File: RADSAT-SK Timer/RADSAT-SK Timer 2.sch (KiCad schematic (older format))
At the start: 50 parts, among them J201 Conn_01x07, J202 Conn_01x05, J203 Conn_01x03, J204 Conn_01x02, J205 Conn_01x02, J206 Conn_01x02, J210 ZX62WRD-B-5PC, Q201 IRLML2060, Q202 IRLML2060, Q203 IRLML2060, Q204 IRLML2060, Q205 IRLML2060, Q206 IRLML2060, SW201 SW_Push, SW202 SW_Push, SW203 SW_Push, SW204 SW_Push, SW205 SW_Push, SW206 SW_Push, U202 LTC3440EMSPBF, U230 CPC1117N, U240 CPC1117N, U250 CPC1117N, U260 CPC1117N

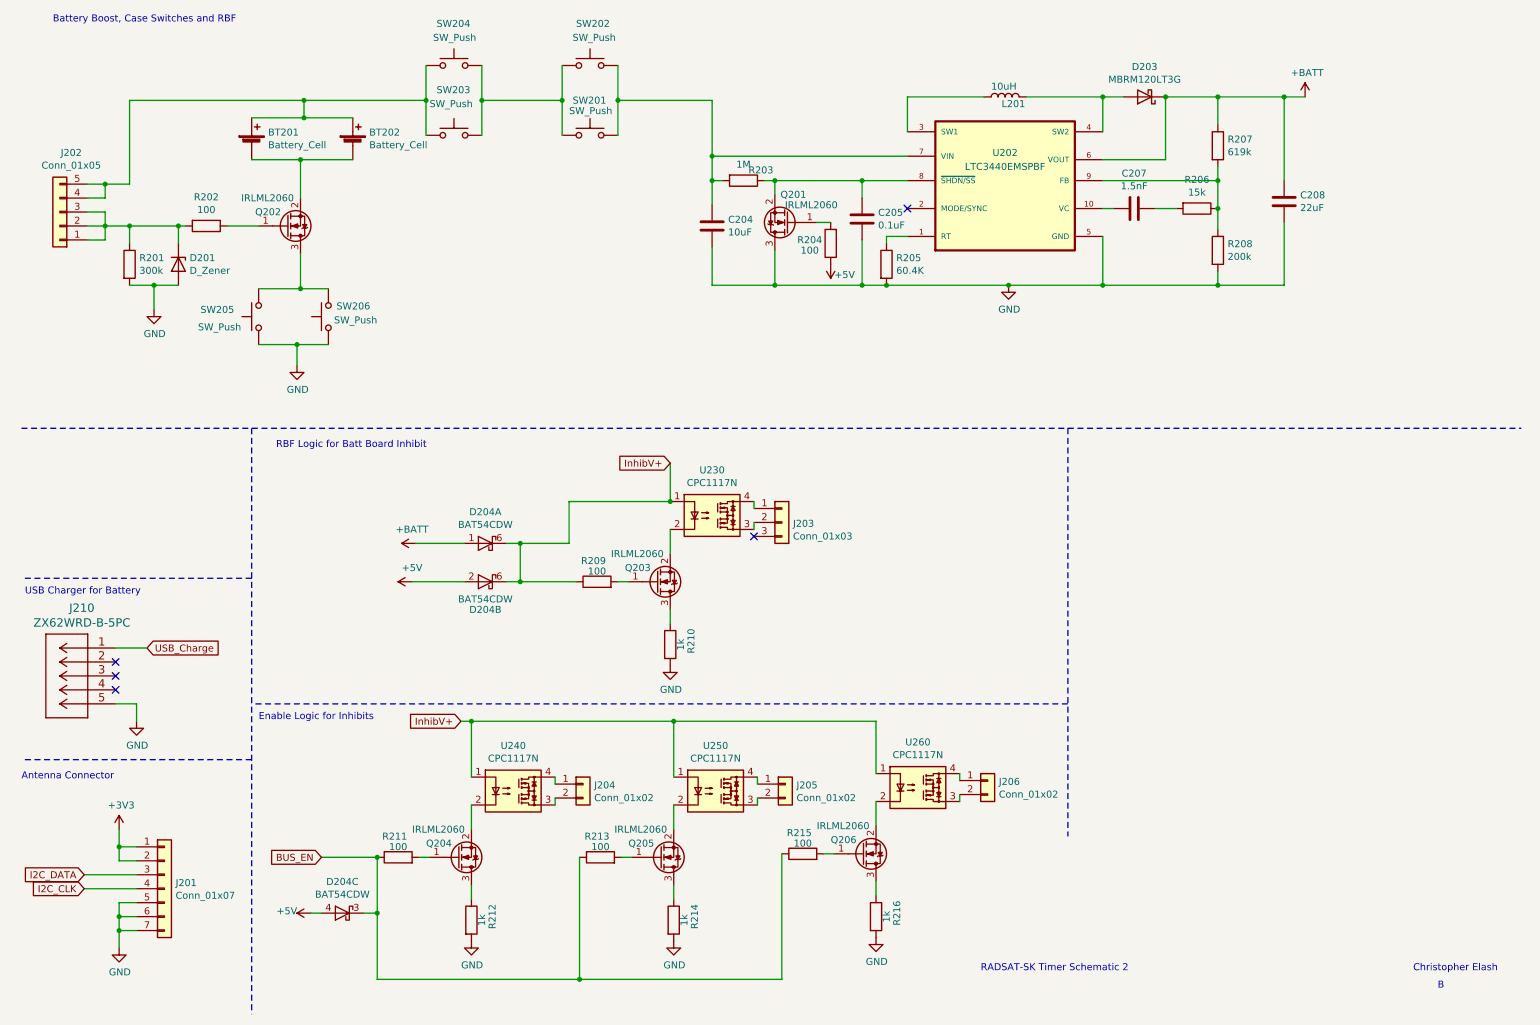
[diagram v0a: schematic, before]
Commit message: Noticed that the source on all of the schematic 2 transistors were wrong and needed to be flipped, except on the rbf where it is intentional q Q ~
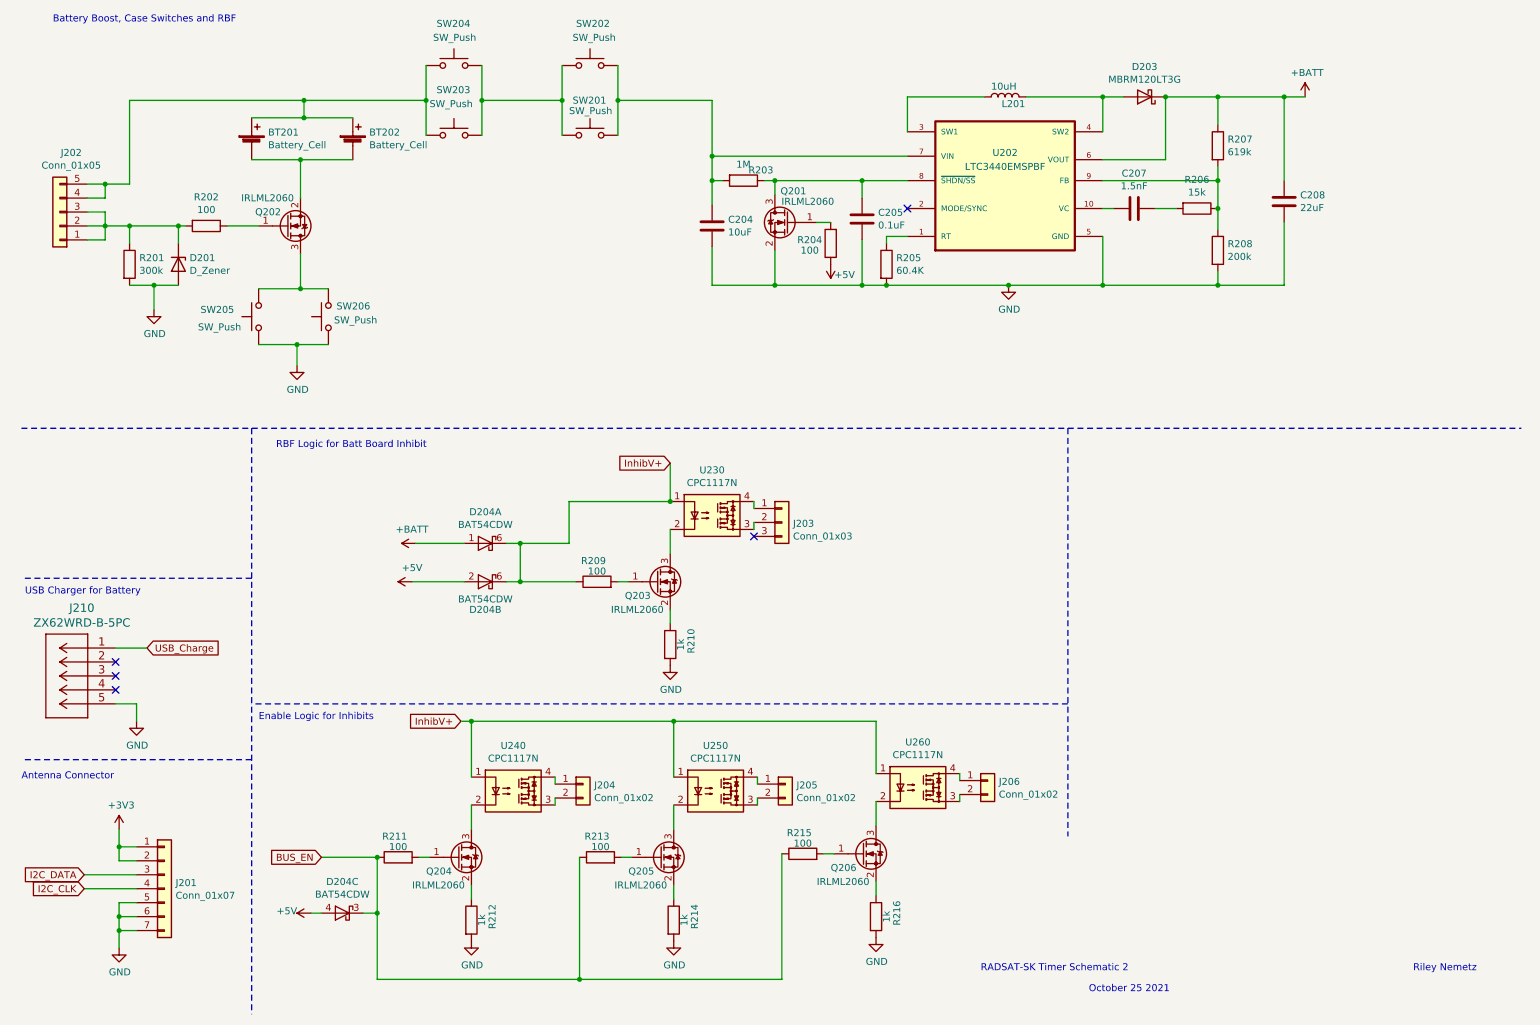
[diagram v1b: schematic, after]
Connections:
- net GND: now also Q201.2 (S); no longer Q201.3 (D)
- net at C205.1, R203.1, U202.8 (~SHDN/SS): now also Q201.3 (D); no longer Q201.2 (S)
- net at Q203.2 (S): now also R210.1; no longer U230.2
- net at Q203.3 (D): now also U230.2; no longer R210.1
- net at Q205.2 (S): now also R214.1; no longer U250.2
- net at Q205.3 (D): now also U250.2; no longer R214.1
- net at Q206.2 (S): now also R216.1; no longer U260.2
- net at Q206.3 (D): now also U260.2; no longer R216.1
- net at Q204.2 (S): now also R212.1; no longer U240.2
- net at Q204.3 (D): now also U240.2; no longer R212.1
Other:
- note added: "October 25 2021"
- note added: "Riley Nemetz"
- note removed: "B"
- note removed: "Christopher Elash"
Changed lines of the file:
@@
 AR Path="/600FFF1C" Ref="Q201"  Part="1"
 AR Path="/602E25D3/600FFF1C" Ref="Q201"  Part="1"
-F 0 "Q201" H 5850 1925 50  0000 L CNN
-F 1 "IRLML2060" H 5625 2000 50  0000 L CNN
+F 0 "Q201" H 5850 2350 50  0000 L CNN
+F 1 "IRLML2060" H 5650 2275 50  0000 L CNN
 F 2 "Package_TO_SOT_SMD:SOT-23_Handsoldering" H 6175 2050 50  0001 L CIN
 F 3 "https://www.infineon.com/dgdl/irlml2060pbf.pdf?fileId=5546d462533600a401535664b7fb25ee" H 5975 2125 50  0001 L CNN
 	1    5975 2125
-	-1   0    0    1
+	-1   0    0    -1
 $EndComp
 Connection ~ 6675 2575
@@
 	2500 1375 2850 1375
 Text Notes 10450 7500 0    50   ~ 0
-Christopher Elash
-Text Notes 10625 7625 0    50   ~ 0
-B
+Riley Nemetz
 Text Notes 700  700  0    50   ~ 0
 Battery Boost, Case Switches and RBF
@@
 F 3 "https://www.infineon.com/dgdl/irlml2060pbf.pdf?fileId=5546d462533600a401535664b7fb25ee" H 5025 4700 50  0001 L CNN
 	1    5025 4700
-	1    0    0    1
+	1    0    0    -1
 $EndComp
 $Comp
@@
 F 3 "https://www.infineon.com/dgdl/irlml2060pbf.pdf?fileId=5546d462533600a401535664b7fb25ee" H 6500 6650 50  0001 L CNN
 	1    6500 6650
-	1    0    0    1
+	1    0    0    -1
 $EndComp
 $Comp
@@
 F 3 "https://www.infineon.com/dgdl/irlml2060pbf.pdf?fileId=5546d462533600a401535664b7fb25ee" H 3600 6675 50  0001 L CNN
 	1    3600 6675
-	1    0    0    1
+	1    0    0    -1
 $EndComp
 Wire Wire Line
@@
 F 3 "https://www.infineon.com/dgdl/irlml2060pbf.pdf?fileId=5546d462533600a401535664b7fb25ee" H 5050 6675 50  0001 L CNN
 	1    5050 6675
-	1    0    0    1
+	1    0    0    -1
 $EndComp
 $Comp
@@
 	1    0    0    -1
 $EndComp
+Text Notes 8125 7650 0    50   ~ 0
+October 25 2021
 $EndSCHEMATC

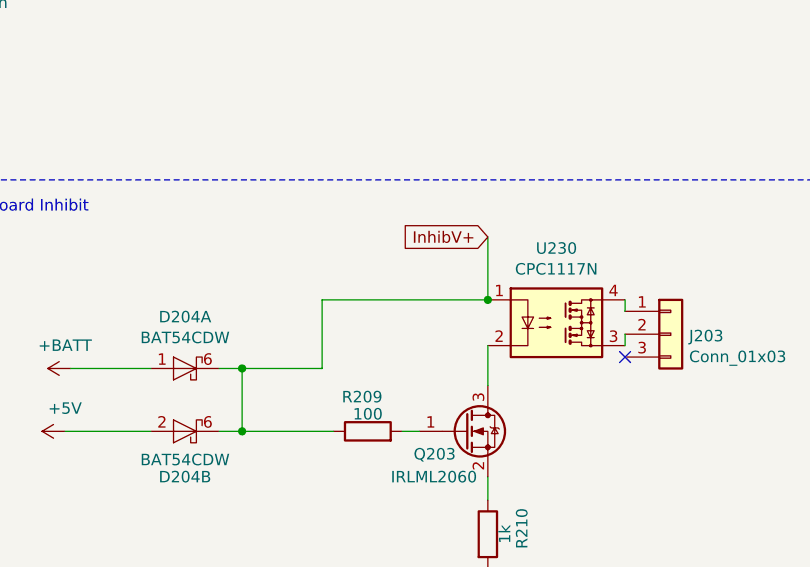
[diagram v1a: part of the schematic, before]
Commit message: Sourced coin cell battery and tantalum caps, still need to footprint coin cell holders
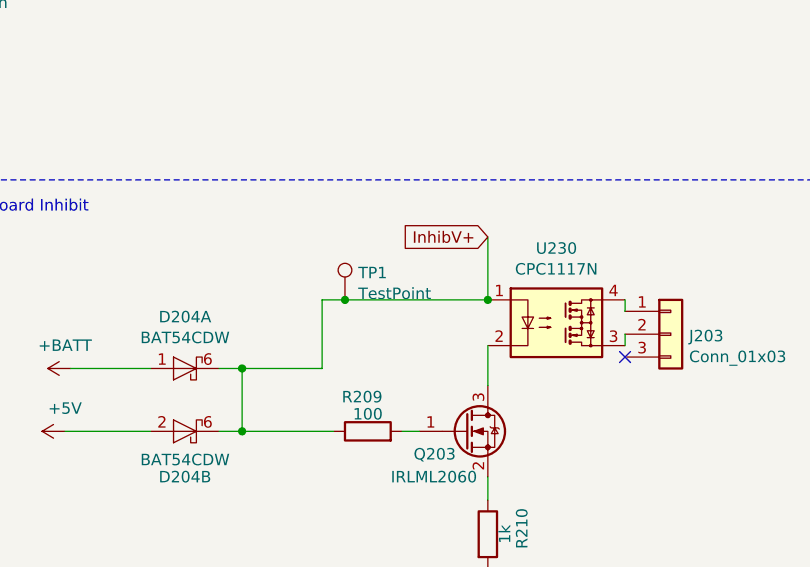
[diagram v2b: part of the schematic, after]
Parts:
- added TP1: TestPoint, TestPoint:TestPoint_Pad_D3.0mm, symbol Connector:TestPoint
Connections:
- net InhibV+: now also TP1.1
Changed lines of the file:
@@
 $EndComp
 $Comp
-L power:GND #PWR?
+L power:GND #PWR0119
 U 1 1 6182F8D4
 P 6600 7250
-F 0 "#PWR?" H 6600 7000 50  0001 C CNN
+F 0 "#PWR0119" H 6600 7000 50  0001 C CNN
 F 1 "GND" H 6605 7077 50  0000 C CNN
 F 2 "" H 6600 7250 50  0001 C CNN
@@
 $EndComp
 $Comp
-L power:GND #PWR?
+L power:GND #PWR0120
 U 1 1 6183DF37
 P 3700 7275
-F 0 "#PWR?" H 3700 7025 50  0001 C CNN
+F 0 "#PWR0120" H 3700 7025 50  0001 C CNN
 F 1 "GND" H 3705 7102 50  0000 C CNN
 F 2 "" H 3700 7275 50  0001 C CNN
@@
 	4775 6675 4850 6675
 $Comp
-L power:GND #PWR?
+L power:GND #PWR0121
 U 1 1 6181C5BF
 P 5150 7275
-F 0 "#PWR?" H 5150 7025 50  0001 C CNN
+F 0 "#PWR0121" H 5150 7025 50  0001 C CNN
 F 1 "GND" H 5155 7102 50  0000 C CNN
 F 2 "" H 5150 7275 50  0001 C CNN
@@
 	4400 4425 4400 4125
 Wire Wire Line
-	4400 4125 5125 4125
+	4400 4125 4500 4125
 Wire Wire Line
 	4050 4425 4400 4425
@@
 Text Notes 8125 7650 0    50   ~ 0
 October 25 2021
+$Comp
+L Connector:TestPoint TP1
+U 1 1 617A6F6B
+P 4500 4125
+F 0 "TP1" H 4558 4243 50  0000 L CNN
+F 1 "TestPoint" H 4558 4152 50  0000 L CNN
+F 2 "TestPoint:TestPoint_Pad_D3.0mm" H 4700 4125 50  0001 C CNN
+F 3 "~" H 4700 4125 50  0001 C CNN
+	1    4500 4125
+	1    0    0    -1
+$EndComp
+Connection ~ 4500 4125
+Wire Wire Line
+	4500 4125 5125 4125
 $EndSCHEMATC

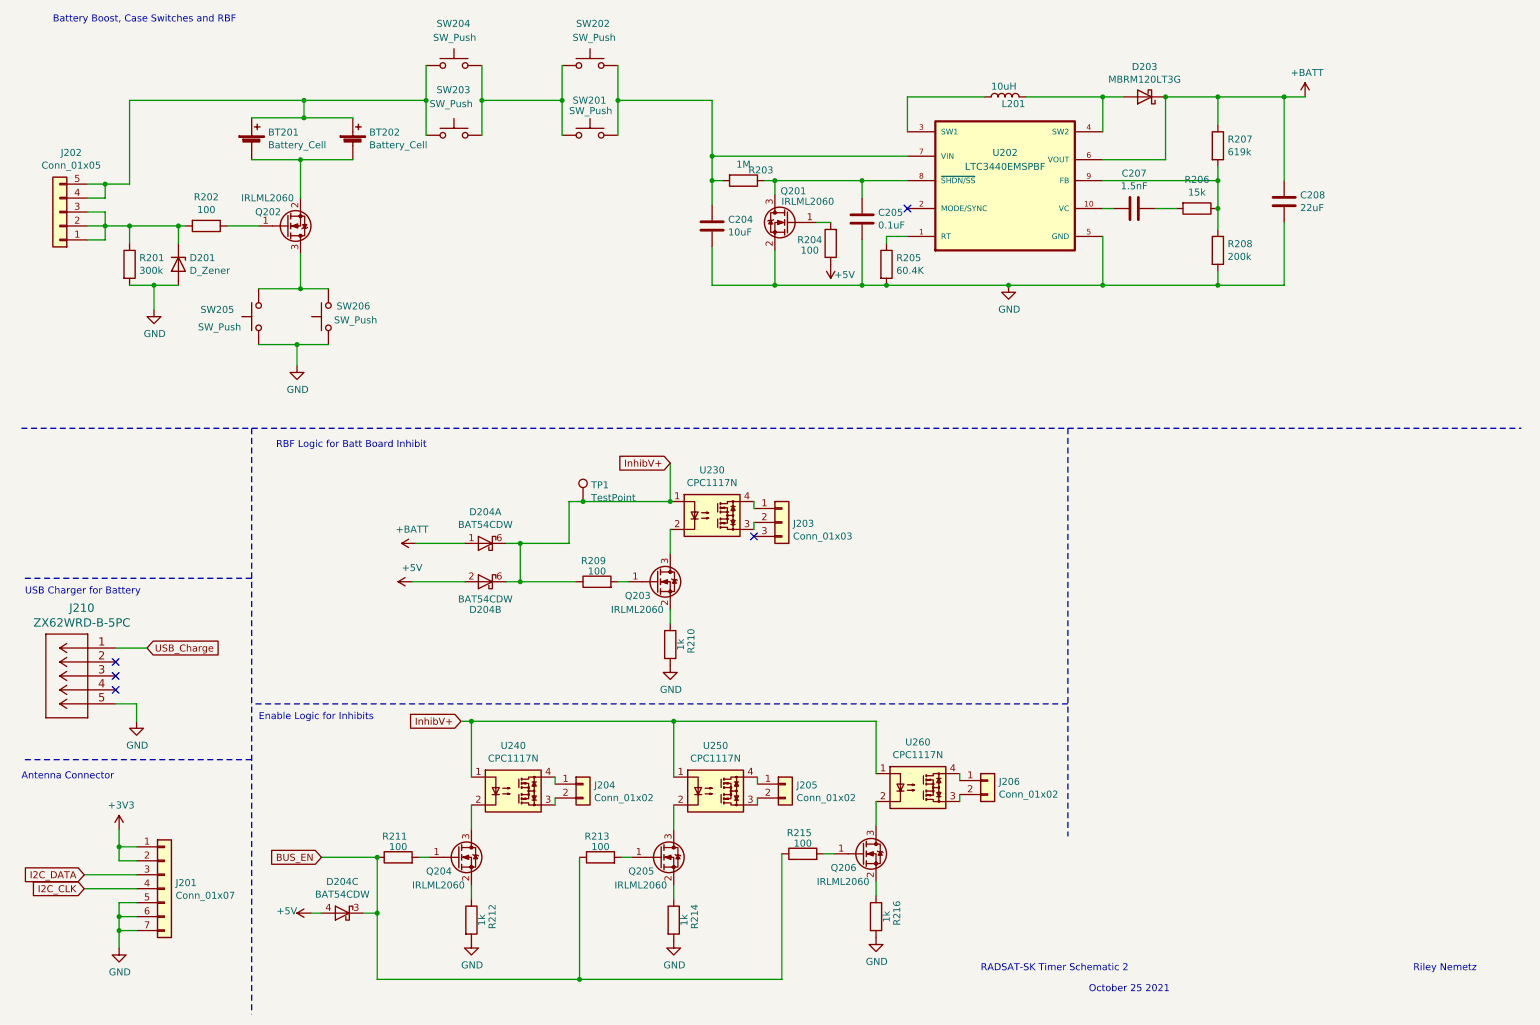
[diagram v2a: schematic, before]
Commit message: the RBF relay transistor was redundant, added in another LED and updated diode configuration, resistor sourcing TBD
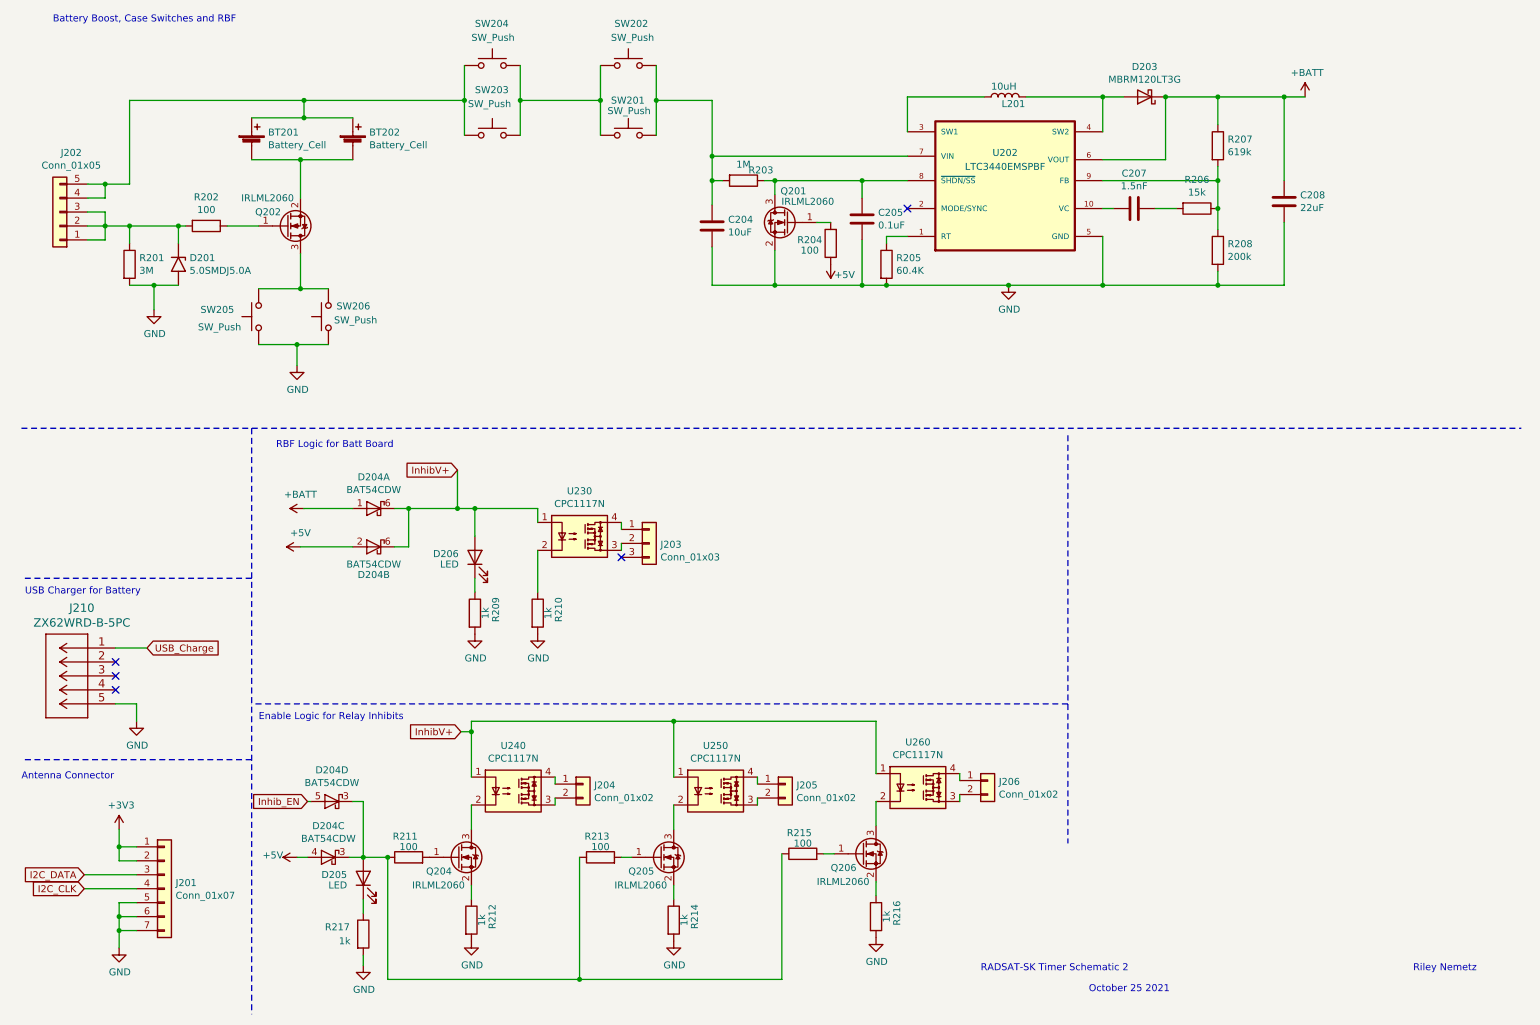
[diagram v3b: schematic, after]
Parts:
- removed D201: D_Zener, Diode_SMD:D_0805_2012Metric, symbol Device:D_Zener
- removed Q203: IRLML2060, Package_TO_SOT_SMD:SOT-23_Handsoldering, symbol Transistor_FET:IRLML2060
- removed TP1: TestPoint, TestPoint:TestPoint_Pad_D3.0mm, symbol Connector:TestPoint
- added D201: 5.0SMDJ5.0A, Diode_SMD:D_SMC_Handsoldering, symbol Diode:SM6T6V8A
- added unit 4 of D204
- added D205, D206: LED, LED_SMD:LED_0603_1608Metric_Pad1.05x0.95mm_HandSolder, symbol Device:LED
- added R217: 1k, Resistor_SMD:R_0805_2012Metric, symbol Device:R
- R201: value 300k -> 3M
- R209: value 100 -> 1k
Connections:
- net GND: now also R209.2, D201.2 (A2), R217.2
- net InhibV+: now also D206.2 (A); no longer R209.1
- net at J202.1 (Pin_1), J202.2 (Pin_2), J202.3 (Pin_3)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: now also D201.1 (A1)
- net at R210.1: now also U230.2
- net BUS_EN: no longer names the net of D204.3 (K), R211.1, R213.1, R215.1
- net BUS_EN: now also D204.3 (K), D205.2 (A)
- new net: D205.1 (K), R217.1
- new net: D206.1 (K), R209.1
- new net Inhib_EN: D204.5 (A)
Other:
- note added: "Enable Logic for Relay Inhibits"
- note added: "RBF Logic for Batt Board"
- note removed: "Enable Logic for Inhibits"
- note removed: "RBF Logic for Batt Board Inhibit"
- moved on the sheet: D204A, D204B, D204C, J203, R210, R211, SW201, SW202, SW203, SW204, U230

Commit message: need to go bakc to previos zener diode for overvoltage
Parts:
- J203: footprint Connector_Hirose:Hirose_DF13-03P-1.25DSA_1x03_P1.25mm_Vertical -> Connector_Hirose:Hirose_DF13C_CL535-0403-5-51_1x03-1MP_P1.25mm_Vertical
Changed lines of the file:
@@
 	4625 1500 4625 1250
-Wire Wire Line
-	4050 1500 4050 1250
 Wire Wire Line
 	2175 3000 2450 3000
@@
 Wire Wire Line
 	2475 1675 2850 1675
-Connection ~ 4050 1250
 Wire Wire Line
 	4050 1250 4050 1000
@@
 F 0 "J203" H 5055 4417 50  0000 L CNN
 F 1 "Conn_01x03" H 5055 4326 50  0000 L CNN
-F 2 "Connector_Hirose:Hirose_DF13-03P-1.25DSA_1x03_P1.25mm_Vertical" H 4975 4425 50  0001 C CNN
+F 2 "Connector_Hirose:Hirose_DF13C_CL535-0403-5-51_1x03-1MP_P1.25mm_Vertical" H 4975 4425 50  0001 C CNN
 F 3 "~" H 4975 4425 50  0001 C CNN
 	1    4975 4425
@@
 Wire Notes Line
 	2125 5975 475  5975
-Wire Wire Line
-	4050 1250 4625 1250
 Wire Wire Line
 	1600 2275 1600 2150
@@
 	3650 1500 3650 1250
 $Comp
-L Switch:SW_Push SW203
-U 1 1 60B0F765
-P 3850 1500
-F 0 "SW203" H 3725 1825 50  0000 L CNN
-F 1 "SW_Push" H 3675 1725 50  0000 L CNN
-F 2 "Connector_Hirose:Hirose_DF13-02P-1.25DSA_1x02_P1.25mm_Vertical" H 3850 1700 50  0001 C CNN
-F 3 "~" H 3850 1700 50  0001 C CNN
-	1    3850 1500
-	1    0    0    -1
-$EndComp
-$Comp
 L Switch:SW_Push SW204
 U 1 1 6012B10E
@@
 Wire Wire Line
 	4175 4475 4175 4775
+Connection ~ 4050 1250
+Wire Wire Line
+	4050 1250 4625 1250
+$Comp
+L Switch:SW_Push SW203
+U 1 1 60B0F765
+P 3850 1500
+F 0 "SW203" H 3725 1825 50  0000 L CNN
+F 1 "SW_Push" H 3675 1725 50  0000 L CNN
+F 2 "Connector_Hirose:Hirose_DF13-02P-1.25DSA_1x02_P1.25mm_Vertical" H 3850 1700 50  0001 C CNN
+F 3 "~" H 3850 1700 50  0001 C CNN
+	1    3850 1500
+	1    0    0    -1
+$EndComp
+Wire Wire Line
+	4050 1500 4050 1250
 $EndSCHEMATC
